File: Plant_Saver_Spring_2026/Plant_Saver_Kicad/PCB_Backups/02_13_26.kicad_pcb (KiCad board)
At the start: 2 copper layers, 80.5 x 83 mm, 113 parts, among them J10 1.25mm, J11 DM3D-SF, J2 SBH11-PBPC-D05-ST-BK, J3 Test, J4 SM04B-SRSS-TB, J6 Conn_01x02_Pin, J7 Conn_01x06_Socket, J8 S3B-PH-K-S, J9 54-00284, Q1 G09P02L, Q10 G09P02L, Q11 ISP12DP06NMXTSA1, Q12 G09P02L, Q2 G09P02L, Q3 ISP12DP06NMXTSA1, Q4 G09P02L, Q5 G09P02L, Q6 G09P02L, Q7 G09P02L, Q8 G09P02L, Q9 G09P02L, SW1 Reset, SW2 1101M2S3AQE2, SW3 Boot, SW4 SA72SB0, U1 CDBA140SL-HF, U10 DW03C, U11 CDBA140SL-HF, U12 LP38511TJ-ADJ/NOPB, U13 MCP73833-xxx-UN, U14 MCP6234, U15 MCP73833-xxx-UN, U16 MCP6547T_I_MS, U2 CDBA140SL-HF, U3 CDBA140SL-HF, U4 CDBA140SL-HF, U5 ESP32-WROOM-32E-N16, U9 CDBA140SL-HF

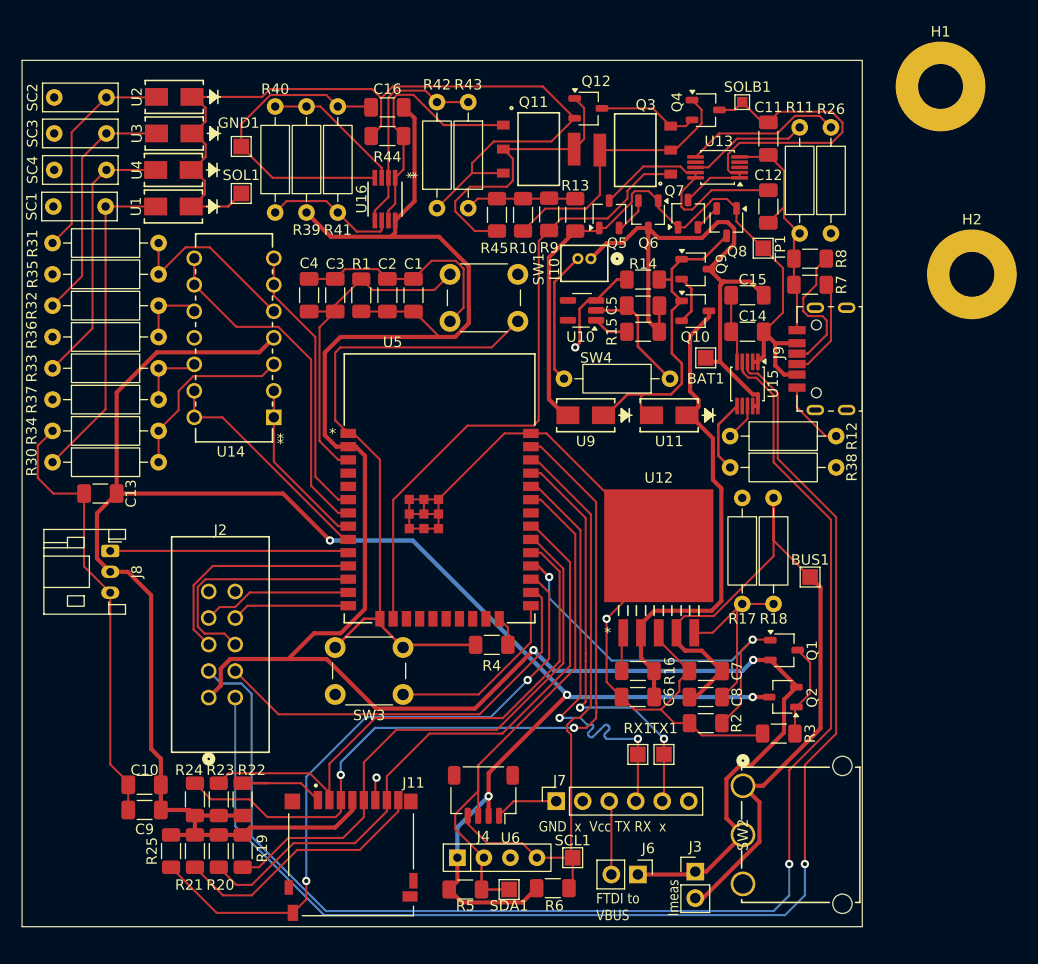
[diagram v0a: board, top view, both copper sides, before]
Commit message: Routing adjustments
Adjusted some lines to improve positions of connectors & uSD. Ground plane needs to be re-added after the top-right corner is improved.
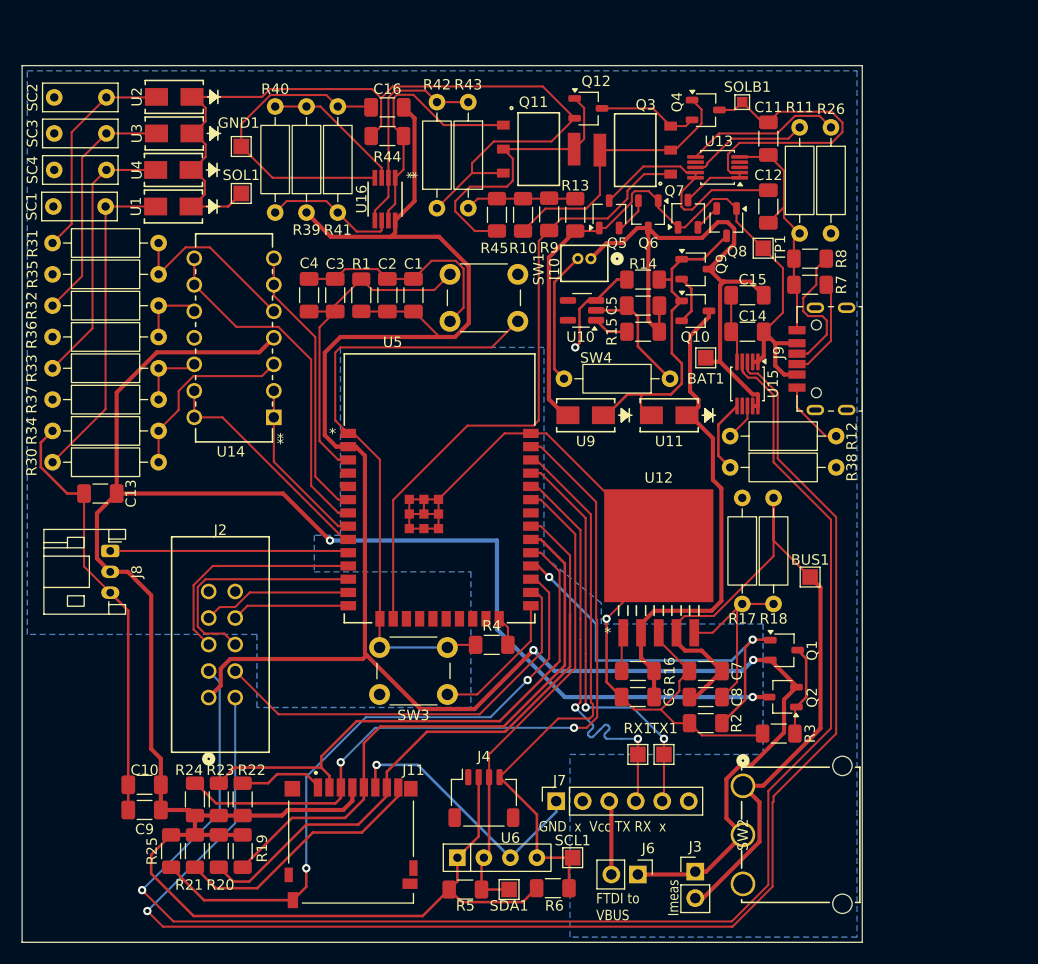
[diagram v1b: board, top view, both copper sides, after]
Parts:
- removed H1, H2: MountingHole_Pad, MountingHole:MountingHole_4.3mm_M4_Pad
- moved SW3 4.25 mm to (67.8, 128.2)
- moved J11 1.22 mm to (58.5, 137.2)
- moved J4 0.30 mm to (71.2, 138.2), turned to 0 degrees
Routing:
- net Vperiph: track 196.2 -> 223.6 mm, vias 4 -> 2
- net STAT1: track 127.5 -> 142.8 mm
- net STAT2: track 130.5 -> 143.8 mm
- net GND: track 308.1 -> 320.8 mm
- net SDA: track 53.5 -> 46.1 mm
- net Vbus: track 192.3 -> 187.8 mm
- net Net-(U5-IO0): track 17.8 -> 13.5 mm
- net SCL: track 58.0 -> 54.4 mm
- net Net-(J7-Pin_4): track 43.0 -> 40.3 mm
- net SPI_MOSI: track 76.0 -> 74.0 mm
- net uSD_DET: track 63.6 -> 61.9 mm
- net uSD_CS: track 54.2 -> 52.6 mm
- net Periph_EN: track 37.9 -> 38.8 mm
- net Net-(J7-Pin_5): track 40.7 -> 40.0 mm
- net SPI_CLK: track 55.2 -> 56.0 mm
- added copper zone on B.Cu, net GND
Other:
- board size 80.5 x 83 mm -> 80.5 x 84 mm
